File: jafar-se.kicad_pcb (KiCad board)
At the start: 2 copper layers, 33 x 41 mm, 15 parts, among them J1 XBOX LPC, J2 JTAG, J3 D0 (1.0-1.4), U1 LC4032V-75TN44I, U2 SST49LF080A-33-4C-NHE

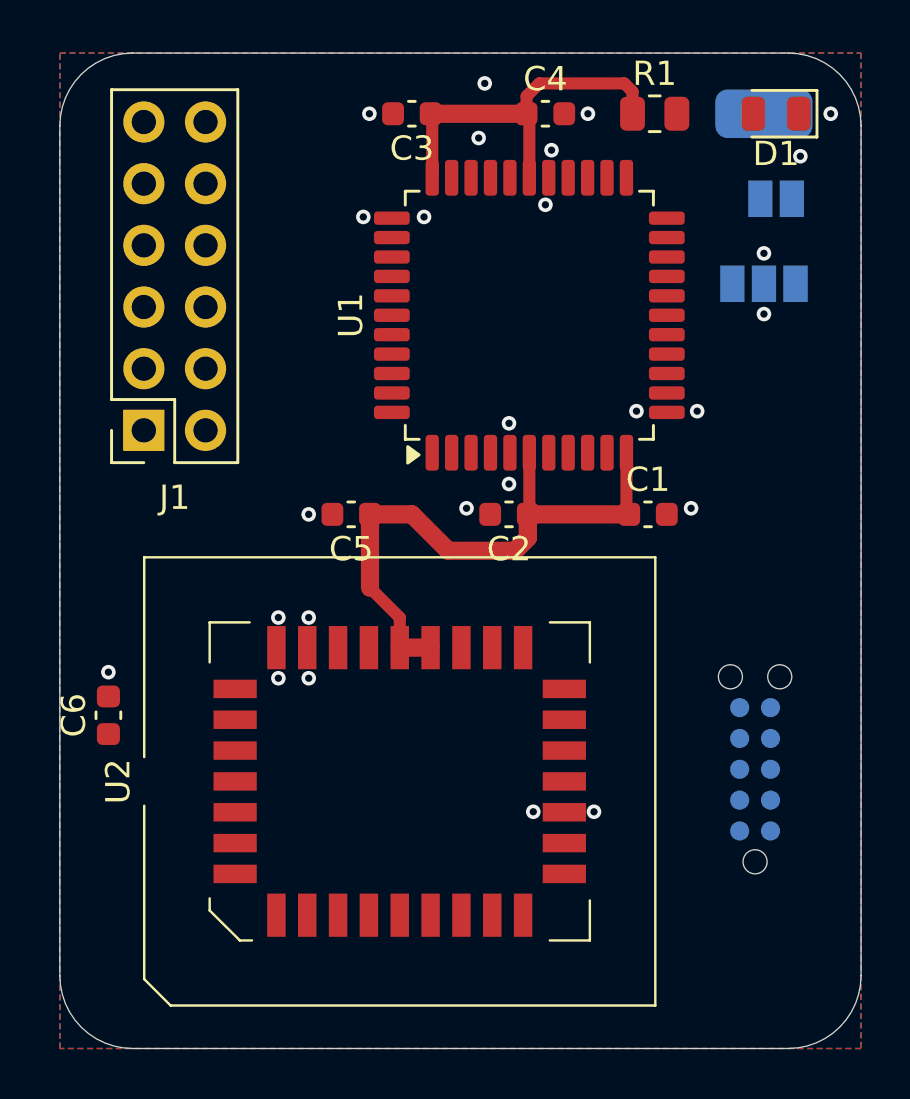
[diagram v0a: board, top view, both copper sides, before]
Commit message: PCB laid out, lots of DRC errors
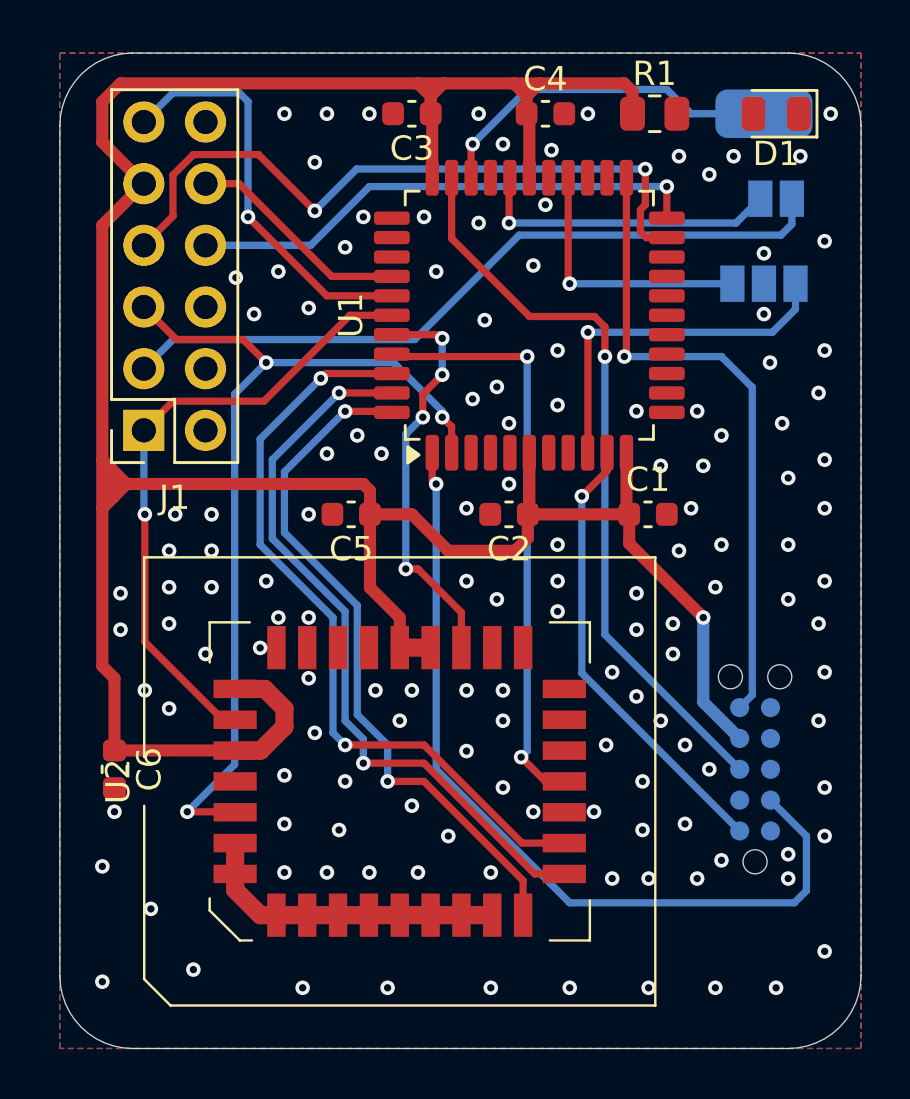
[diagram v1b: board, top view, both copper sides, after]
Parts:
- moved C6 2.24 mm to (122.2, 76.5), turned to -90 degrees
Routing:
- net +3V3: track 40.6 -> 135.9 mm, vias 0 -> 1
- net /~{XLRESET}: track 0.00 -> 37.8 mm, vias 0 -> 3
- net /TDI: track 0.00 -> 35.2 mm, vias 0 -> 1
- net /FLAD2: track 0.00 -> 31.3 mm, vias 0 -> 2
- net /TDO: track 0.00 -> 30.8 mm, vias 0 -> 1
- net /FLAD1: track 0.00 -> 30.3 mm, vias 0 -> 2
- net /~{XLFRAME}: track 0.00 -> 30.2 mm
- net /XLAD3: track 0.00 -> 28.7 mm, vias 0 -> 2
- net /FLAD0: track 0.00 -> 28.7 mm, vias 0 -> 2
- net /TMS: track 0.00 -> 26.6 mm, vias 0 -> 1
- net /XLCLK: track 0.00 -> 26.0 mm, vias 0 -> 1
- net /FLAD3: track 0.00 -> 24.4 mm, vias 0 -> 2
- net /XLAD2: track 0.00 -> 21.3 mm, vias 0 -> 1
- net /TCK: track 0.00 -> 18.7 mm, vias 0 -> 1
- net /XLAD0: track 0.00 -> 17.0 mm, vias 0 -> 1
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
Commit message: Cleanup some DRC
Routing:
- net GND: track 0.00 -> 1.80 mm, vias 139 -> 137
- net /TDI: track 35.2 -> 36.3 mm
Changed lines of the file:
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@@
 		(capping no)
 		(filling no)
+		(zone_defaults)
 		(pcbplotparams
 			(layerselection 0x00000000_00000000_55555555_5755f5ff)
@@
 	)
 	(via
-		(at 151.5 79.25)
-		(size 0.6)
-		(drill 0.3)
-		(layers "F.Cu" "B.Cu")
-		(free yes)
-		(net "GND")
-	)
-	(via
 		(at 151.5 59.25)
 		(size 0.6)
@@
 	)
 	(via
-		(at 150 80)
+		(at 150.25 79.75)
 		(size 0.6)
 		(drill 0.3)
@@
 	)
 	(via
-		(at 151.5 77.25)
-		(size 0.6)
-		(drill 0.3)
-		(layers "F.Cu" "B.Cu")
-		(free yes)
-		(net "GND")
-	)
-	(via
 		(at 147 69)
 		(size 0.6)
@@
 	)
 	(via
-		(at 150 81)
+		(at 149.75 81)
 		(size 0.6)
 		(drill 0.3)
@@
 	)
 	(segment
+		(start 148 77.77)
+		(end 149.27 79.04)
+		(width 0.5)
+		(layer "B.Cu")
+		(net "GND")
+	)
+	(segment
 		(start 136.1375 62.3875)
 		(end 136.1375 63.4625)
@@
 	(segment
 		(start 128.5 59.75)
+		(end 127.75 60.5)
+		(width 0.3)
+		(layer "B.Cu")
+		(net "/~{XLRESET}")
+	)
+	(segment
+		(start 128.5 59.75)
 		(end 133.75 59.75)
 		(width 0.3)
@@
 	)
 	(segment
+		(start 127.75 71.080761)
+		(end 127.6 71.230761)
+		(width 0.3)
+		(layer "B.Cu")
+		(net "/~{XLRESET}")
+	)
+	(segment
+		(start 127.6 71.769239)
+		(end 127.75 71.919239)
+		(width 0.3)
+		(layer "B.Cu")
+		(net "/~{XLRESET}")
+	)
+	(segment
 		(start 135.75 61.75)
 		(end 135.75 62)
@@
 	)
 	(segment
-		(start 127.2 61.05)
-		(end 127.2 76.3)
+		(start 127.75 71.919239)
+		(end 127.75 75.75)
 		(width 0.3)
 		(layer "B.Cu")
@@
 	)
 	(segment
-		(start 128.5 59.75)
-		(end 127.2 61.05)
+		(start 127.6 71.230761)
+		(end 127.6 71.769239)
 		(width 0.3)
 		(layer "B.Cu")
@@
 	)
 	(segment
-		(start 127.2 76.3)
-		(end 125.25 78.25)
+		(start 127.75 60.5)
+		(end 127.75 71.080761)
 		(width 0.3)
 		(layer "B.Cu")
@@
 	)
 	(segment
+		(start 127.75 75.75)
+		(end 125.25 78.25)
+		(width 0.3)
+		(layer "B.Cu")
+		(net "/~{XLRESET}")
+	)
+	(segment
 		(start 131.752983 61.758949)
 		(end 133.633949 61.758949)
@@
 	)
 	(segment
-		(start 125.502943 51.18)
-		(end 128.18 51.18)
+		(start 127.197057 51.88)
+		(end 127.587106 51.88)
+		(width 0.3)
+		(layer "F.Cu")
+		(net "/XLAD3")
+	)
+	(segment
+		(start 124.66 52.022943)
+		(end 125.502943 51.18)
 		(width 0.3)
 		(layer "F.Cu")
@@
 	)
 	(segment
-		(start 128.18 51.18)
-		(end 130.5 53.5)
+		(start 123.46 54.92)
+		(end 124.66 53.72)
 		(width 0.3)
 		(layer "F.Cu")
@@
 	)
 	(segment
-		(start 144.1125 53.25676)
-		(end 143.9125 53.45676)
+		(start 126.497057 51.18)
+		(end 127.197057 51.88)
 		(width 0.3)
 		(layer "F.Cu")
@@
 	)
 	(segment
-		(start 123.46 54.92)
-		(end 124.66 53.72)
+		(start 127.587106 51.88)
+		(end 129.207106 53.5)
 		(width 0.3)
 		(layer "F.Cu")
@@
 	)
 	(segment
-		(start 143.9125 54.3625)
-		(end 144.15 54.6)
+		(start 125.502943 51.18)
+		(end 126.497057 51.18)
+		(width 0.3)
+		(layer "F.Cu")
+		(net "/XLAD3")
+	)
+	(segment
+		(start 144.1125 53.25676)
+		(end 143.9125 53.45676)
+		(width 0.3)
+		(layer "F.Cu")
+		(net "/XLAD3")
+	)
+	(segment
+		(start 129.207106 53.5)
+		(end 130.5 53.5)
 		(width 0.3)
 		(layer "F.Cu")
@@
 	)
 	(segment
-		(start 124.66 52.022943)
-		(end 125.502943 51.18)
+		(start 143.9125 54.3625)
+		(end 144.15 54.6)
 		(width 0.3)
 		(layer "F.Cu")
@@
 	)
 	(segment
-		(start 150.75 79.25)
-		(end 150.75 81.5)
+		(start 141 82)
+		(end 135.5 76.5)
 		(width 0.3)
 		(layer "B.Cu")
@@
 	)
 	(segment
-		(start 135.5 76.5)
-		(end 135.5 64.75)
+		(start 149.27 77.77)
+		(end 150.52 77.77)
+		(width 0.3)
+		(layer "B.Cu")
+		(net "/TDI")
+	)
+	(segment
+		(start 150.52 77.77)
+		(end 151.25 78.5)
 		(width 0.3)
 		(layer "B.Cu")
@@
 	)
 	(segment
-		(start 150.75 81.5)
+		(start 151.25 81)
 		(end 150.25 82)
 		(width 0.3)
@@
 	)
 	(segment
-		(start 141 82)
-		(end 135.5 76.5)
+		(start 151.25 78.5)
+		(end 151.25 81)
 		(width 0.3)
 		(layer "B.Cu")
@@
 	)
 	(segment
-		(start 149.27 77.77)
-		(end 150.75 79.25)
+		(start 135.5 76.5)
+		(end 135.5 64.75)
 		(width 0.3)
 		(layer "B.Cu")

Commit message: No DRC errors, only warnings
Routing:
- net +3V3: track 135.9 -> 143.3 mm
- net /LED: track 0.00 -> 3.15 mm
- net GND: vias 137 -> 135
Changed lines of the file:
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@@
 			)
 		)
+		(solder_mask_margin 0.05)
 		(attr smd)
 		(duplicate_pad_numbers_are_jumpers no)
@@
 	)
 	(segment
-		(start 138.7 48.25)
-		(end 139.75 48.25)
-		(width 0.5)
+		(start 128.08 79.54)
+		(end 129.25 78.37)
+		(width 0.75)
 		(layer "F.Cu")
 		(net "+3V3")
 	)
 	(segment
-		(start 132.5 64.75)
-		(end 132.775 65.025)
+		(start 138.7 48.25)
+		(end 139.75 48.25)
 		(width 0.5)
 		(layer "F.Cu")
@@
 	)
 	(segment
-		(start 127.215 75.725)
-		(end 127.22 75.73)
+		(start 132.5 64.75)
+		(end 132.775 65.025)
 		(width 0.5)
 		(layer "F.Cu")
@@
 	)
 	(segment
+		(start 128.73 75.73)
+		(end 128.27 75.73)
+		(width 0.75)
+		(layer "F.Cu")
+		(net "+3V3")
+	)
+	(segment
 		(start 134 71.49)
 		(end 134 70.25)
@@
 	)
 	(segment
+		(start 129.25 78.37)
+		(end 129.25 76.25)
+		(width 0.75)
+		(layer "F.Cu")
+		(net "+3V3")
+	)
+	(segment
+		(start 129.25 76.25)
+		(end 128.73 75.73)
+		(width 0.75)
+		(layer "F.Cu")
+		(net "+3V3")
+	)
+	(segment
 		(start 121.75 65.75)
 		(end 121.75 72.25)
@@
 	)
 	(segment
-		(start 122.25 75.725)
-		(end 127.215 75.725)
-		(width 0.5)
+		(start 129.25 76.25)
+		(end 129.25 74.75)
+		(width 0.75)
 		(layer "F.Cu")
 		(net "+3V3")
@@
 	)
 	(segment
+		(start 127.22 79.54)
+		(end 128.08 79.54)
+		(width 0.75)
+		(layer "F.Cu")
+		(net "+3V3")
+	)
+	(segment
 		(start 143.3375 65.8875)
 		(end 143.45 66)
@@
 	)
 	(segment
+		(start 127.215 75.725)
+		(end 127.22 75.73)
+		(width 0.5)
+		(layer "F.Cu")
+		(net "+3V3")
+	)
+	(segment
 		(start 134 71.49)
 		(end 135.27 71.49)
@@
 	)
 	(segment
+		(start 122.25 75.725)
+		(end 127.215 75.725)
+		(width 0.5)
+		(layer "F.Cu")
+		(net "+3V3")
+	)
+	(segment
 		(start 134 70.25)
 		(end 132.775 69.025)
@@
 	)
 	(via
-		(at 129.25 78.75)
-		(size 0.6)
-		(drill 0.3)
-		(layers "F.Cu" "B.Cu")
-		(free yes)
-		(net "GND")
-	)
-	(via
-		(at 129.25 76.75)
-		(size 0.6)
-		(drill 0.3)
-		(layers "F.Cu" "B.Cu")
-		(free yes)
-		(net "GND")
-	)
-	(via
 		(at 140.5 67.25)
 		(size 0.6)
@@
 		(net "/TDO")
 	)
+	(segment
+		(start 145.4125 49.5)
+		(end 148.5625 49.5)
+		(width 0.5)
+		(layer "F.Cu")
+		(net "/LED")
+	)
 	(zone

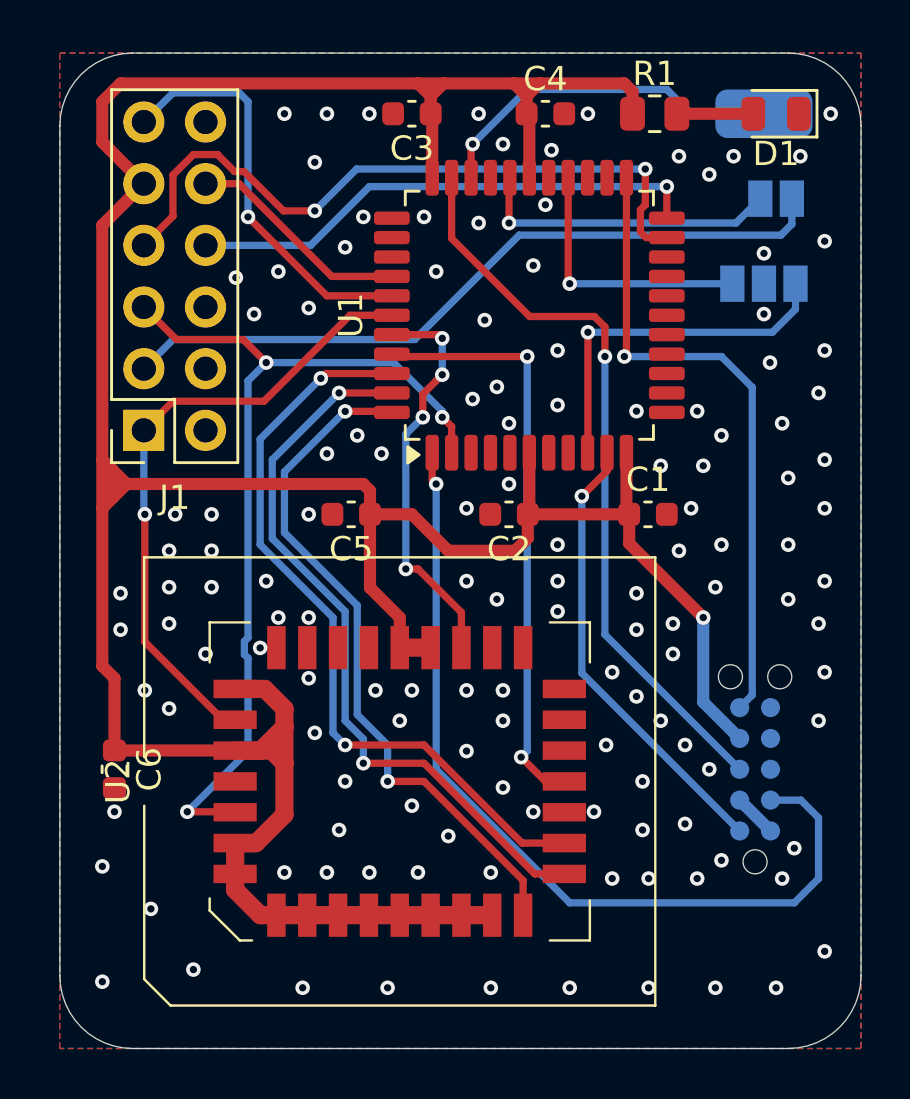
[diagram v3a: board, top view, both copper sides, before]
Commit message: New board layout, more intact bottom layer
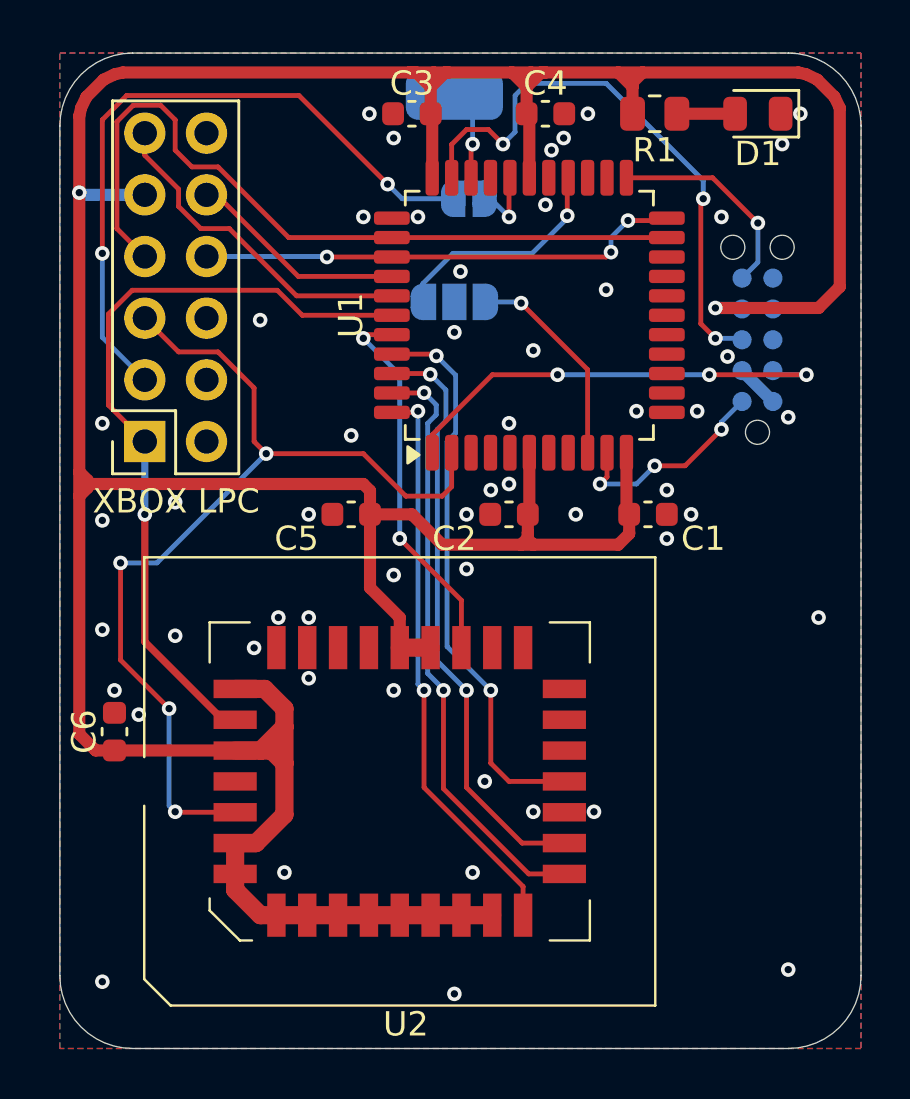
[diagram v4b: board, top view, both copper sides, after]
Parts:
- JP1: footprint Jumper:SolderJumper-3_P1.3mm_Open_Pad1.0x1.5mm -> Jumper:SolderJumper-3_P1.3mm_Open_RoundedPad1.0x1.5mm
- JP2: footprint Jumper:SolderJumper-2_P1.3mm_Open_Pad1.0x1.5mm -> Jumper:SolderJumper-2_P1.3mm_Open_RoundedPad1.0x1.5mm
- moved J2 17.7 mm to (148.7, 58.8)
- moved J3 12.8 mm to (136.2, 48.8)
- moved JP1 12.8 mm to (136.2, 57.2)
- moved JP2 12.7 mm to (136.8, 53.0), turned to 0 degrees
- moved C6 1.55 mm to (122.2, 75.0), turned to 90 degrees
- moved D1 0.75 mm to (148.8, 49.5)
- moved J1 0.46 mm to (123.5, 63.0)
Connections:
- U1 pad 35: unconnected-(U1-B12-Pad35) -> /XLAD3
- U1 pad 36: unconnected-(U1-B13-Pad36) -> /XLAD2
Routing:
- net +3V3: track 143.3 -> 163.7 mm, vias 1 -> 2
- net /TMS: track 26.6 -> 8.72 mm
- net /TDI: track 36.3 -> 18.6 mm, vias 1 -> 3
- net /D0: track 14.8 -> 3.72 mm
- net /TCK: track 18.7 -> 8.84 mm, vias 1 -> 3
- net /XLFRAME_L1: track 12.6 -> 2.94 mm
- net /TDO: track 30.8 -> 23.7 mm, vias 1 -> 3
- net /FLAD2: track 31.3 -> 24.5 mm
- net /H0: track 15.0 -> 8.78 mm
- net /XLCLK: track 26.0 -> 31.7 mm
- net /FLAD1: track 30.3 -> 24.7 mm
- net /FLAD0: track 28.7 -> 23.6 mm
- net /XLAD3: track 28.7 -> 32.0 mm, vias 2 -> 0
- net /XLAD0: track 17.0 -> 13.9 mm, vias 1 -> 0
- net /~{XLRESET}: track 37.9 -> 40.1 mm, vias 3 -> 4
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
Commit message: Moved pads and rerouted
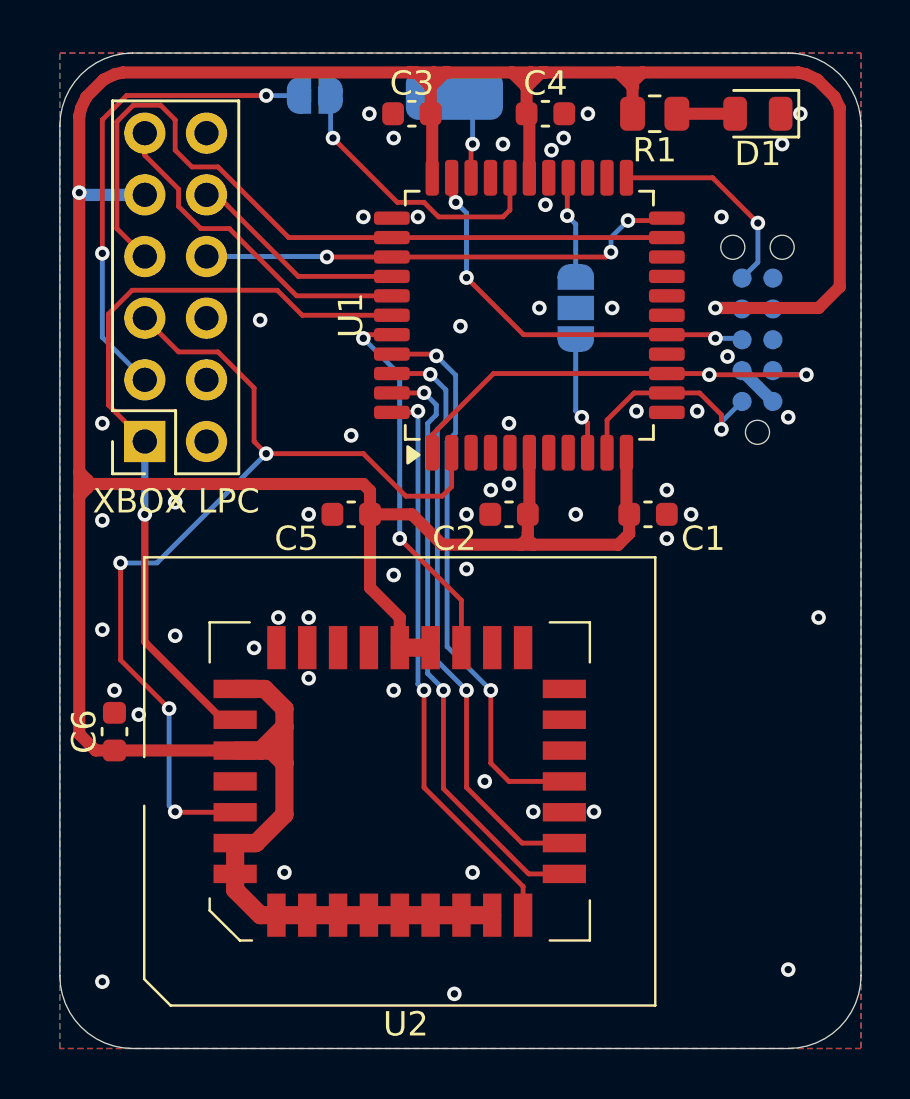
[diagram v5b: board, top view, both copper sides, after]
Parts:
- added G***: LOGO, LOGO, B.Cu at (136.8, 69.2)
- moved JP2 7.64 mm to (130.5, 48.8)
- moved JP1 5.01 mm to (141.2, 57.5), turned to 90 degrees
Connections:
- U1 pad 13: unconnected-(U1-A12-Pad13) -> /TCK
- U1 pad 14: unconnected-(U1-A13-Pad14) -> /TDI
- U1 pad 16: unconnected-(U1-A15-Pad16) -> /TDO
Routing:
- net /XLFRAME_L1: track 2.94 -> 11.9 mm
- net /~{XLFRAME}: track 28.1 -> 19.9 mm
- net /TDO: track 23.7 -> 16.8 mm
- net /BT: track 9.50 -> 4.32 mm
- net /H0: track 8.78 -> 4.88 mm
- net /TCK: track 8.84 -> 9.00 mm, vias 3 -> 1
- net /TDI: track 18.6 -> 18.7 mm, vias 3 -> 2
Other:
- board text added: "Jafar - Socket Edition Rev A Made by Kekule-OXC Adapted by Clegg"

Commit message: Finish BOM minus socket
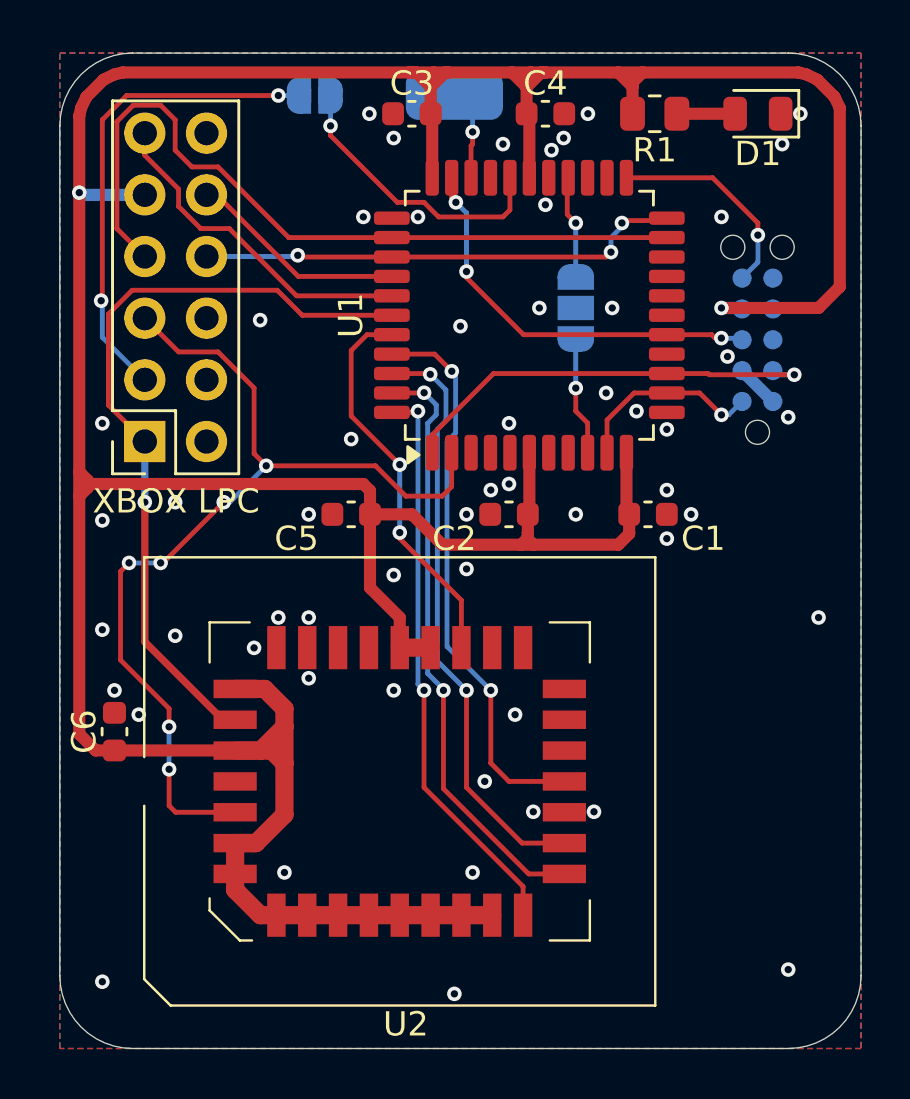
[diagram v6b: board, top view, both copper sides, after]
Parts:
- J3: value D0 (1.0-1.4) -> D0
- JP2: value LFRAME (1.6) -> L1
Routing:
- net /TCK: track 9.00 -> 7.97 mm
- net /TDI: track 18.7 -> 17.7 mm, vias 2 -> 1
- net +3V3: track 163.7 -> 163.2 mm
- net /~{XLRESET}: track 40.1 -> 39.8 mm, vias 4 -> 6
- net GND: vias 53 -> 55

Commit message: Add PLCC-32 socket to schematic so that it shows up in the BOM
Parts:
- removed U2: SST49LF080A-33-4C-NHE, Library:PLCC-32_SMD-Socket
- added J4: PLCC-32 Socket, Library:PLCC-32_SMD-Socket, F.Cu at (134.0, 77.0)
